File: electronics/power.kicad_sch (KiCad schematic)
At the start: 10 parts, among them J1 9V regulated input, Q1 CSD18540Q5B, U4 LM74700QDBVRQ1

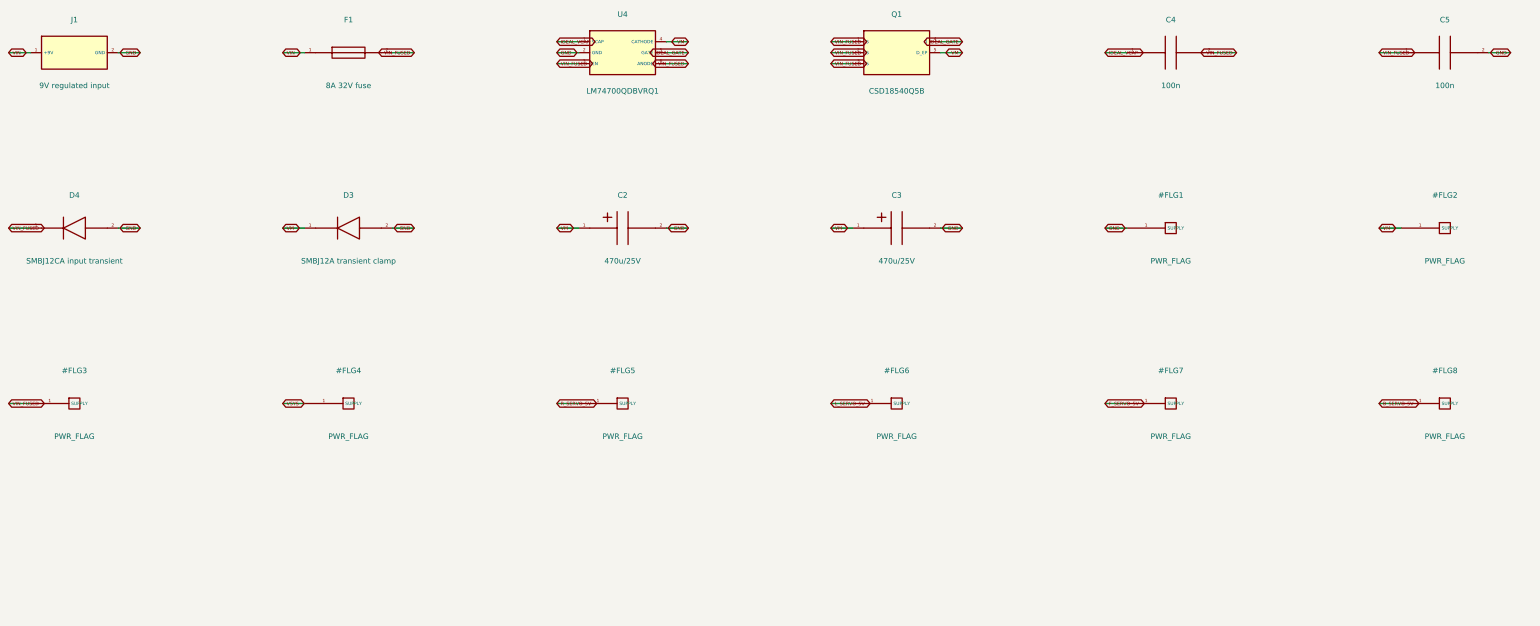
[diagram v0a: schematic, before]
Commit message: Integrate onboard RP2040 and drawing-based EV3 jacks on A1 PCB
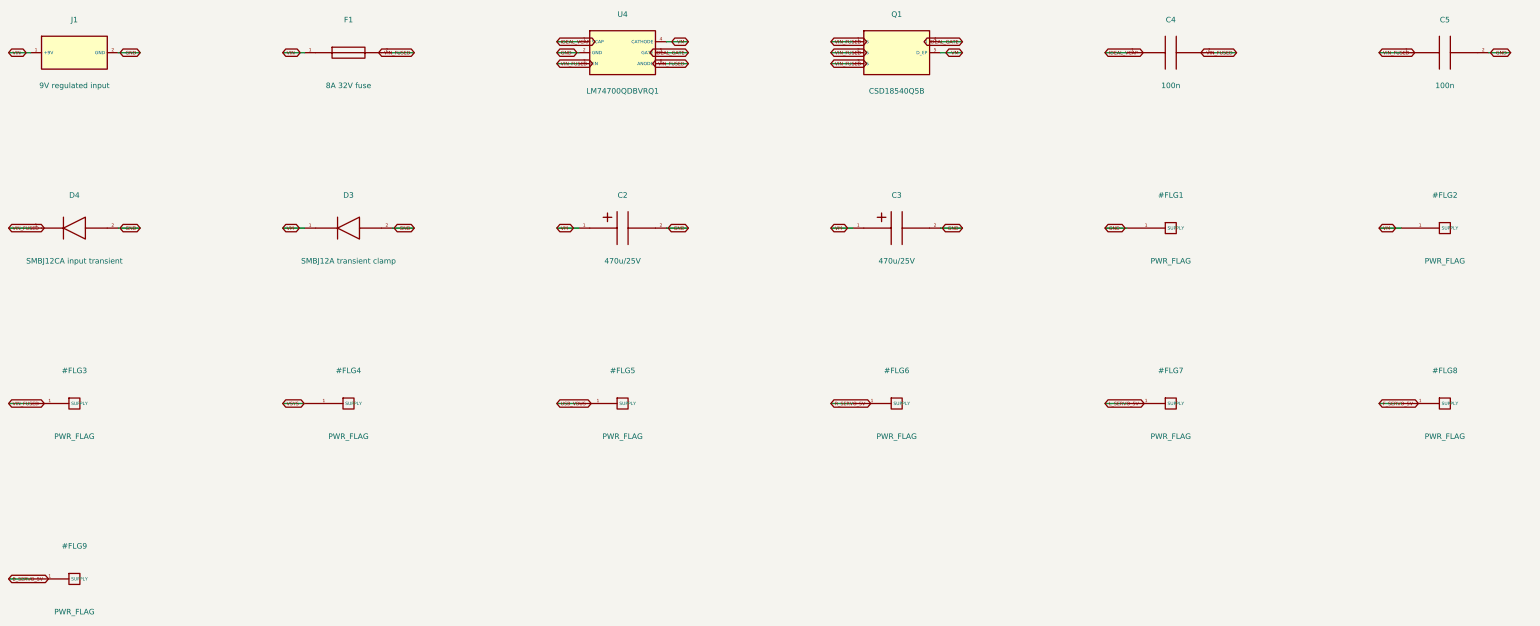
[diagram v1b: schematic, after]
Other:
- title: Quadcuber A0 / power / ENGINEERING HOLD -> Quadcuber A1 / power / ENGINEERING HOLD

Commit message: Correct audited power BOM and add bounded VM discharge protection
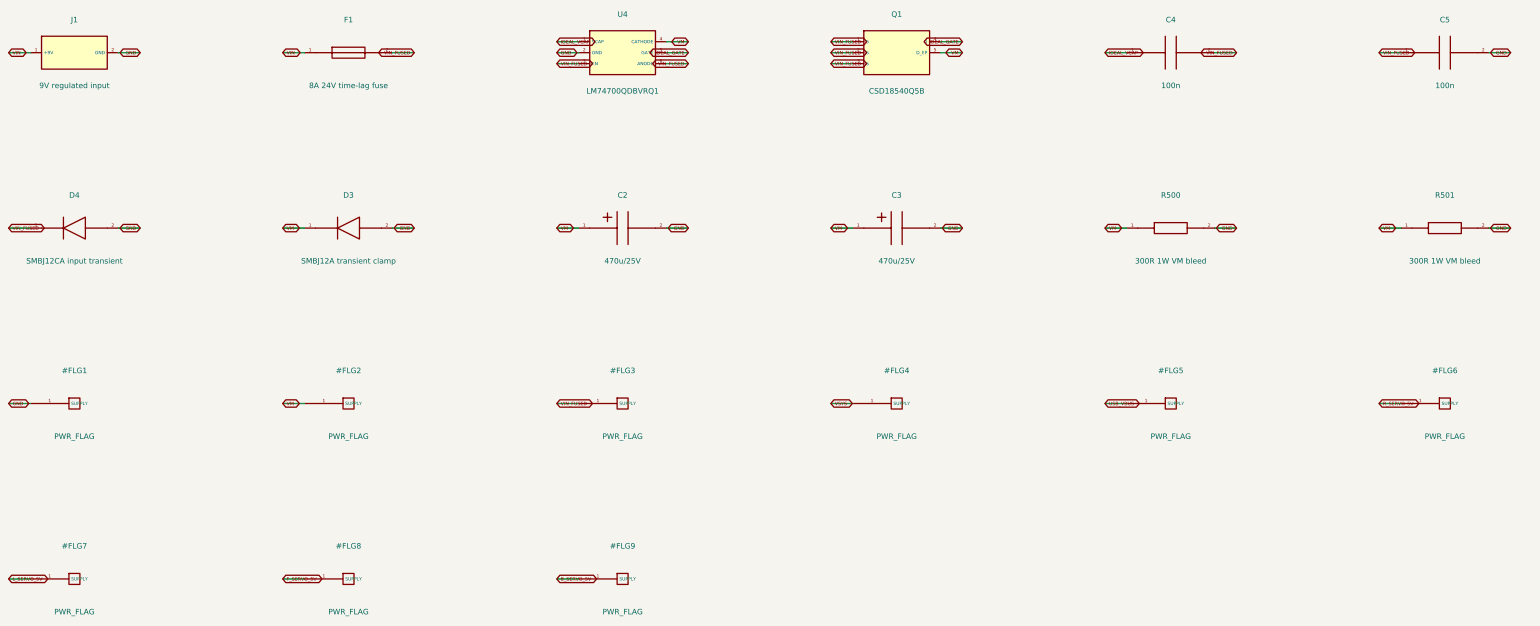
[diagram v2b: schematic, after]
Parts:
- added R500: 300R 1W VM bleed, Quadcuber:R_2512_6332Metric, symbol Quadcuber:R500
- added R501: 300R 1W VM bleed, Quadcuber:R_2512_6332Metric, symbol Quadcuber:R501
- F1: value 8A 32V fuse -> 8A 24V time-lag fuse; footprint Quadcuber:Fuse_1206_3216Metric -> Quadcuber:Fuse_Littelfuse_407_1206; MPN 0467008.NR -> 0407008.WR
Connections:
- net GND: now also R500.2, R501.2
- net VM: now also R500.1, R501.1

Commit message: Migrate A1 to KiCad 10 and record blocked vendor-model transients
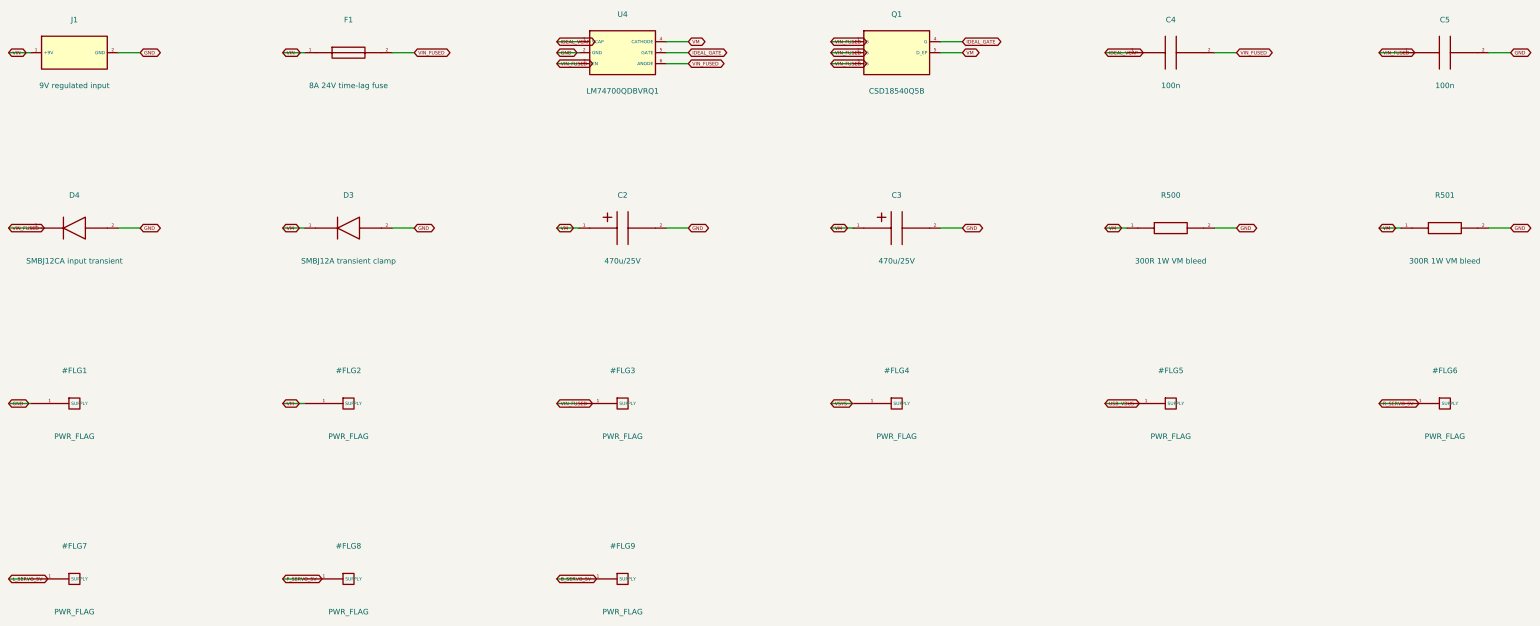
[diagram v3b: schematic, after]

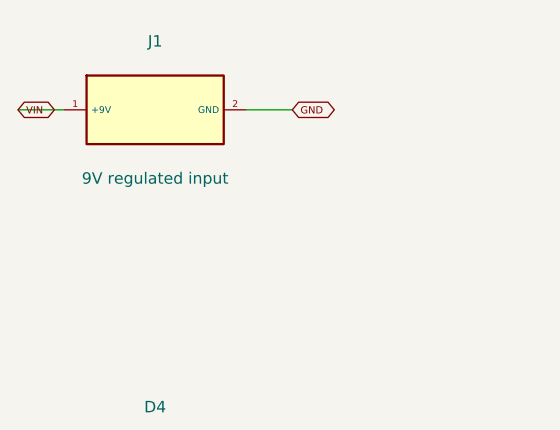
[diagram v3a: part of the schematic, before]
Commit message: Replace J1 with center-positive RASPC722X DC input
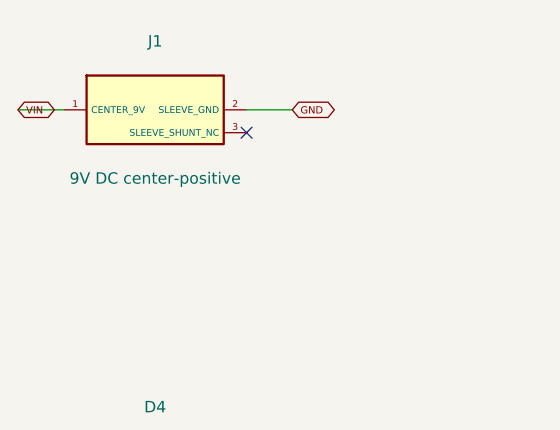
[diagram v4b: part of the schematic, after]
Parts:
- J1: value 9V regulated input -> 9V DC center-positive; footprint Quadcuber:TerminalBlock_Phoenix_MKDS-1,5-2-5.08_1x02_P5.08mm_Horizontal -> Quadcuber:Jack_DC_Switchcraft_RASPC722X; MPN 1715721 -> RASPC722X; Manufacturer Phoenix Contact -> Switchcraft
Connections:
- no-connect marks 0 -> 1
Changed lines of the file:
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@@
 			)
 		)
-		(property "Value" "9V regulated input"
+		(property "Value" "9V DC center-positive"
 			(at 35.56 45.72 0)
 			(show_name no)
@@
 			)
 		)
-		(property "Footprint" "Quadcuber:TerminalBlock_Phoenix_MKDS-1,5-2-5.08_1x02_P5.08mm_Horizontal"
+		(property "Footprint" "Quadcuber:Jack_DC_Switchcraft_RASPC722X"
 			(at 35.56 38.1 0)
 			(hide yes)
@@
 			)
 		)
-		(property "MPN" "1715721"
+		(property "MPN" "RASPC722X"
 			(at 35.56 38.1 0)
 			(hide yes)
@@
 			)
 		)
-		(property "Manufacturer" "Phoenix Contact"
+		(property "Manufacturer" "Switchcraft"
 			(at 35.56 38.1 0)
 			(hide yes)
@@
 			)
 		)
-	)
+	(pin "3"))
 	(symbol
 		(lib_id "Quadcuber:#FLG1")
@@
 		)
 	)
+(no_connect (at 45.72 40.64))
 )
